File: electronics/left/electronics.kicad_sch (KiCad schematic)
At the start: 85 parts, among them J1 USB_C_Receptacle_USB2.0, J2 Battery Connector, SW1 SW_Reset, U1 Choc v1 Socket, U10 Choc v1 Socket, U11 Choc v1 Socket, U12 Choc v1 Socket, U13 Choc v1 Socket, U14 Choc v1 Socket, U15 Choc v1 Socket, U16 Choc v1 Socket, U17 Choc v1 Socket, U18 Choc v1 Socket, U19 Choc v1 Socket, U2 Choc v1 Socket, U20 Choc v1 Socket, U21 Choc v1 Socket, U22 nRF52840, U23 ESDR0502NMUTAG, U24 BQ24075RGT, U3 Choc v1 Socket, U4 Choc v1 Socket, U5 Choc v1 Socket, U6 Choc v1 Socket, U7 Choc v1 Socket, U8 Choc v1 Socket, U9 Choc v1 Socket, Y1 32.768 kHz, Y2 32MHz

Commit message: Component metadata updates:
* Use official footprints for 0402 caps and resistors.
* Use correct JLC and LCSC part numbers for the choc switches.
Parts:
- C1, C10, C11, C12, C13, C14, C15, C16, C17, C18, C19, C2, C20, C21, C22, C23, C24, C25, C26, C3, C4, C5, C6, C7, C8, C9: footprint lib:C_0402_1005Metric -> Capacitor_SMD:C_0402_1005Metric
- R1, R10, R11, R12, R2, R3, R4, R5, R6, R7, R8, R9: footprint lib:R_0402_1005Metric -> Resistor_SMD:R_0402_1005Metric
- U1, U10, U11, U12, U13, U14, U15, U16, U17, U18, U19, U2, U20, U21, U3, U4, U5, U6, U7, U8, U9: value Choc v1 Socket -> CPG135001S30; JLC Part C2803348 -> C5333465; LCSC Part C2803348 -> C5333465

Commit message: Value update for battery connector and reset switch.
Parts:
- J2: value Battery Connector -> Molex_781710002; symbol Molex_Pico-EZmate_78171-0002_1x02-1MP_P1.20mm_Vertical:Battery Connector -> Molex_Pico-EZmate_78171-0002_1x02-1MP_P1.20mm_Vertical:Molex_781710002
- SW1: value SW_Reset -> EVQPUC02K
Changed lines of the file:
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@@
     )
   )
-  (symbol (lib_id "Molex_Pico-EZmate_78171-0002_1x02-1MP_P1.20mm_Vertical:Battery Connector") (at 249.428 309.88 180) (unit 1)
+  (symbol (lib_id "Molex_Pico-EZmate_78171-0002_1x02-1MP_P1.20mm_Vertical:Molex_781710002") (at 249.428 309.88 180) (unit 1)
     (in_bom yes) (on_board yes) (dnp no)
     (property "Reference" "J2" (at 249.428 299.085 0)
       (effects (font (size 1.27 1.27)))
     )
-    (property "Value" "Battery Connector" (at 249.428 301.625 0)
+    (property "Value" "Molex_781710002" (at 249.555 302.006 0)
       (effects (font (size 1.27 1.27)))
     )
@@
       (effects (font (size 1.27 1.27)) hide)
     )
-    (property "Manufacturer Part" "Molex_Pico-EZmate_78171-0002" (at 249.428 295.91 0)
-      (effects (font (size 1.27 1.27)) hide)
-    )
-    (property "LCSC Part" "C505023" (at 249.428 309.88 0)
-      (effects (font (size 1.27 1.27)) hide)
-    )
-    (property "JLC Part" "C505023" (at 249.428 309.88 0)
+    (property "Manufacturer Part" "Molex_Pico-EZmate_78171-0002" (at 248.793 292.735 0)
+      (effects (font (size 1.27 1.27)) hide)
+    )
+    (property "LCSC Part" "C505023" (at 250.063 295.91 0)
+      (effects (font (size 1.27 1.27)) hide)
+    )
+    (property "JLC Part" "C505023" (at 250.063 295.91 0)
       (effects (font (size 1.27 1.27)) hide)
     )
@@
       (effects (font (size 1.27 1.27)) (justify right))
     )
-    (property "Value" "SW_Reset" (at 60.96 254 0)
+    (property "Value" "EVQPUC02K" (at 60.96 254 0)
       (effects (font (size 1.27 1.27)) (justify right))
     )
@@
       (effects (font (size 1.27 1.27)) hide)
     )
-    (property "Datasheet" "~" (at 57.15 257.81 0)
-      (effects (font (size 1.27 1.27)) hide)
-    )
+    (property "Datasheet" "" (at 57.15 257.81 0)
+      (effects (font (size 1.27 1.27)) hide)
+    )

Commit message: BOM value updates:
USB C Receptable
Molex connector.
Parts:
- J1: LCSC Part (none) -> C2988367; Manufacturer Part (none) -> GT-USB-9014C
- J2: Manufacturer Part Molex_Pico-EZmate_78171-0002 -> 781710002
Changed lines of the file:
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@@
       (effects (font (size 1.27 1.27)) hide)
     )
-    (property "Manufacturer Part" "Molex_Pico-EZmate_78171-0002" (at 248.793 292.735 0)
+    (property "Manufacturer Part" "781710002" (at 248.793 292.735 0)
       (effects (font (size 1.27 1.27)) hide)
     )
@@
       (effects (font (size 1.27 1.27)) hide)
     )
+    (property "LCSC Part" "C2988367" (at 192.405 253.746 90)
+      (effects (font (size 1.27 1.27)) hide)
+    )
+    (property "Manufacturer Part" "GT-USB-9014C" (at 192.405 253.746 90)
+      (effects (font (size 1.27 1.27)) hide)
+    )

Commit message: Add JLC Part number to LEDs
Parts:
- D1: JLC Part (none) -> C605447
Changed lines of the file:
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@@
+      (effects (font (size 1.27 1.27)) hide)
+    )
+    (property "JLC Part" "C605447" (at 189.23 189.23 0)
       (effects (font (size 1.27 1.27)) hide)
     )

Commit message: Use official symbol for charging IC.
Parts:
- U24: footprint lib:VQFN-16-1EP_3x3mm_P0.5mm_EP1.6x1.6mm -> Package_DFN_QFN:VQFN-16-1EP_3x3mm_P0.5mm_EP1.6x1.6mm; symbol BQ24075RGT:BQ24075RGT -> Battery_Management:BQ24075RGT
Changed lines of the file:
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@@
     )
   )
-  (symbol (lib_id "BQ24075RGT:BQ24075RGT") (at 204.343 327.66 0) (unit 1)
+  (symbol (lib_id "Battery_Management:BQ24075RGT") (at 204.343 327.66 0) (unit 1)
     (in_bom yes) (on_board yes) (dnp no)
     (property "Reference" "U24" (at 202.438 347.345 0)
@@
       (effects (font (size 1.27 1.27)) (justify left))
     )
-    (property "Footprint" "lib:VQFN-16-1EP_3x3mm_P0.5mm_EP1.6x1.6mm" (at 211.963 341.63 0)
+    (property "Footprint" "Package_DFN_QFN:VQFN-16-1EP_3x3mm_P0.5mm_EP1.6x1.6mm" (at 211.963 341.63 0)
       (effects (font (size 1.27 1.27)) (justify left) hide)
     )

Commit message: electronics/right: Fix schema and PCB references parity.
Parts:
- renumbered U1 to SW1, U10 to SW10, U11 to SW11, U12 to SW12, U13 to SW13, U14 to SW14, U15 to SW15, U16 to SW16, U17 to SW17, U18 to SW18, U19 to SW19, U2 to SW2, U20 to SW20, U21 to SW21, U3 to SW3, U4 to SW4, U5 to SW5, U6 to SW6, U7 to SW7, U8 to SW8, U9 to SW9
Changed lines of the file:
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@@
   (symbol (lib_id "Kailh_socket_PG1350:Choc v1 Socket") (at 262.89 30.48 0) (unit 1)
     (in_bom yes) (on_board yes) (dnp no) (fields_autoplaced)
-    (property "Reference" "U6" (at 263.525 21.751 0)
+    (property "Reference" "SW6" (at 263.525 21.751 0)
       (effects (font (size 1.27 1.27)))
     )
@@
   (symbol (lib_id "Kailh_socket_PG1350:Choc v1 Socket") (at 179.07 60.96 0) (unit 1)
     (in_bom yes) (on_board yes) (dnp no) (fields_autoplaced)
-    (property "Reference" "U15" (at 179.705 52.231 0)
+    (property "Reference" "SW15" (at 179.705 52.231 0)
       (effects (font (size 1.27 1.27)))
     )
@@
   (symbol (lib_id "Kailh_socket_PG1350:Choc v1 Socket") (at 120.65 60.96 0) (unit 1)
     (in_bom yes) (on_board yes) (dnp no) (fields_autoplaced)
-    (property "Reference" "U13" (at 121.285 51.435 0)
+    (property "Reference" "SW13" (at 121.285 51.435 0)
       (effects (font (size 1.27 1.27)))
     )
@@
   (symbol (lib_id "Kailh_socket_PG1350:Choc v1 Socket") (at 262.89 60.96 0) (unit 1)
     (in_bom yes) (on_board yes) (dnp no) (fields_autoplaced)
-    (property "Reference" "U18" (at 263.525 52.231 0)
+    (property "Reference" "SW18" (at 263.525 52.231 0)
       (effects (font (size 1.27 1.27)))
     )
@@
   (symbol (lib_id "Kailh_socket_PG1350:Choc v1 Socket") (at 236.22 76.2 0) (unit 1)
     (in_bom yes) (on_board yes) (dnp no) (fields_autoplaced)
-    (property "Reference" "U20" (at 236.855 67.471 0)
+    (property "Reference" "SW20" (at 236.855 67.471 0)
       (effects (font (size 1.27 1.27)))
     )
@@
   (symbol (lib_id "Kailh_socket_PG1350:Choc v1 Socket") (at 149.86 60.96 0) (unit 1)
     (in_bom yes) (on_board yes) (dnp no) (fields_autoplaced)
-    (property "Reference" "U14" (at 150.495 52.231 0)
+    (property "Reference" "SW14" (at 150.495 52.231 0)
       (effects (font (size 1.27 1.27)))
     )
@@
   (symbol (lib_id "Kailh_socket_PG1350:Choc v1 Socket") (at 149.86 45.72 0) (unit 1)
     (in_bom yes) (on_board yes) (dnp no) (fields_autoplaced)
-    (property "Reference" "U8" (at 150.495 36.991 0)
+    (property "Reference" "SW8" (at 150.495 36.991 0)
       (effects (font (size 1.27 1.27)))
     )
@@
   (symbol (lib_id "Kailh_socket_PG1350:Choc v1 Socket") (at 234.95 45.72 0) (unit 1)
     (in_bom yes) (on_board yes) (dnp no) (fields_autoplaced)
-    (property "Reference" "U11" (at 235.585 36.991 0)
+    (property "Reference" "SW11" (at 235.585 36.991 0)
       (effects (font (size 1.27 1.27)))
     )
@@
   (symbol (lib_id "Kailh_socket_PG1350:Choc v1 Socket") (at 234.95 30.48 0) (unit 1)
     (in_bom yes) (on_board yes) (dnp no) (fields_autoplaced)
-    (property "Reference" "U5" (at 235.585 20.955 0)
+    (property "Reference" "SW5" (at 235.585 20.955 0)
       (effects (font (size 1.27 1.27)))
     )
@@
   (symbol (lib_id "Kailh_socket_PG1350:Choc v1 Socket") (at 208.28 60.96 0) (unit 1)
     (in_bom yes) (on_board yes) (dnp no) (fields_autoplaced)
-    (property "Reference" "U16" (at 208.915 52.231 0)
+    (property "Reference" "SW16" (at 208.915 52.231 0)
       (effects (font (size 1.27 1.27)))
     )
@@
   (symbol (lib_id "Kailh_socket_PG1350:Choc v1 Socket") (at 236.22 60.96 0) (unit 1)
     (in_bom yes) (on_board yes) (dnp no) (fields_autoplaced)
-    (property "Reference" "U17" (at 236.855 52.231 0)
+    (property "Reference" "SW17" (at 236.855 52.231 0)
       (effects (font (size 1.27 1.27)))
     )
@@
   (symbol (lib_id "Kailh_socket_PG1350:Choc v1 Socket") (at 208.28 45.72 0) (unit 1)
     (in_bom yes) (on_board yes) (dnp no) (fields_autoplaced)
-    (property "Reference" "U10" (at 208.915 36.991 0)
+    (property "Reference" "SW10" (at 208.915 36.991 0)
       (effects (font (size 1.27 1.27)))
     )
@@
   (symbol (lib_id "Kailh_socket_PG1350:Choc v1 Socket") (at 179.07 30.48 0) (unit 1)
     (in_bom yes) (on_board yes) (dnp no) (fields_autoplaced)
-    (property "Reference" "U3" (at 179.705 21.751 0)
+    (property "Reference" "SW3" (at 179.705 21.751 0)
       (effects (font (size 1.27 1.27)))
     )
@@
   (symbol (lib_id "Kailh_socket_PG1350:Choc v1 Socket") (at 207.01 30.48 0) (unit 1)
     (in_bom yes) (on_board yes) (dnp no) (fields_autoplaced)
-    (property "Reference" "U4" (at 207.645 21.751 0)
+    (property "Reference" "SW4" (at 207.645 21.751 0)
       (effects (font (size 1.27 1.27)))
     )
@@
   (symbol (lib_id "Kailh_socket_PG1350:Choc v1 Socket") (at 208.28 76.2 0) (unit 1)
     (in_bom yes) (on_board yes) (dnp no) (fields_autoplaced)
-    (property "Reference" "U19" (at 208.915 67.471 0)
+    (property "Reference" "SW19" (at 208.915 67.471 0)
       (effects (font (size 1.27 1.27)))
     )
@@
   (symbol (lib_id "Kailh_socket_PG1350:Choc v1 Socket") (at 149.86 30.48 0) (unit 1)
     (in_bom yes) (on_board yes) (dnp no) (fields_autoplaced)
-    (property "Reference" "U2" (at 150.495 21.751 0)
+    (property "Reference" "SW2" (at 150.495 21.751 0)
       (effects (font (size 1.27 1.27)))
     )
@@
   (symbol (lib_id "Kailh_socket_PG1350:Choc v1 Socket") (at 264.16 76.2 0) (unit 1)
     (in_bom yes) (on_board yes) (dnp no) (fields_autoplaced)
-    (property "Reference" "U21" (at 264.795 67.471 0)
+    (property "Reference" "SW21" (at 264.795 67.471 0)
       (effects (font (size 1.27 1.27)))
     )
@@
   (symbol (lib_id "Kailh_socket_PG1350:Choc v1 Socket") (at 262.89 45.72 0) (unit 1)
     (in_bom yes) (on_board yes) (dnp no) (fields_autoplaced)
-    (property "Reference" "U12" (at 263.525 36.195 0)
+    (property "Reference" "SW12" (at 263.525 36.195 0)
       (effects (font (size 1.27 1.27)))
     )
@@
   (symbol (lib_id "Kailh_socket_PG1350:Choc v1 Socket") (at 120.65 30.48 0) (unit 1)
     (in_bom yes) (on_board yes) (dnp no) (fields_autoplaced)
-    (property "Reference" "U1" (at 121.285 20.955 0)
+    (property "Reference" "SW1" (at 121.285 20.955 0)
       (effects (font (size 1.27 1.27)))
     )
@@
   (symbol (lib_id "Kailh_socket_PG1350:Choc v1 Socket") (at 179.07 45.72 0) (unit 1)
     (in_bom yes) (on_board yes) (dnp no) (fields_autoplaced)
-    (property "Reference" "U9" (at 179.705 36.991 0)
+    (property "Reference" "SW9" (at 179.705 36.991 0)
       (effects (font (size 1.27 1.27)))
     )
@@
   (symbol (lib_id "Kailh_socket_PG1350:Choc v1 Socket") (at 120.65 45.72 0) (unit 1)
     (in_bom yes) (on_board yes) (dnp no) (fields_autoplaced)
-    (property "Reference" "U7" (at 121.285 36.195 0)
+    (property "Reference" "SW7" (at 121.285 36.195 0)
       (effects (font (size 1.27 1.27)))
     )

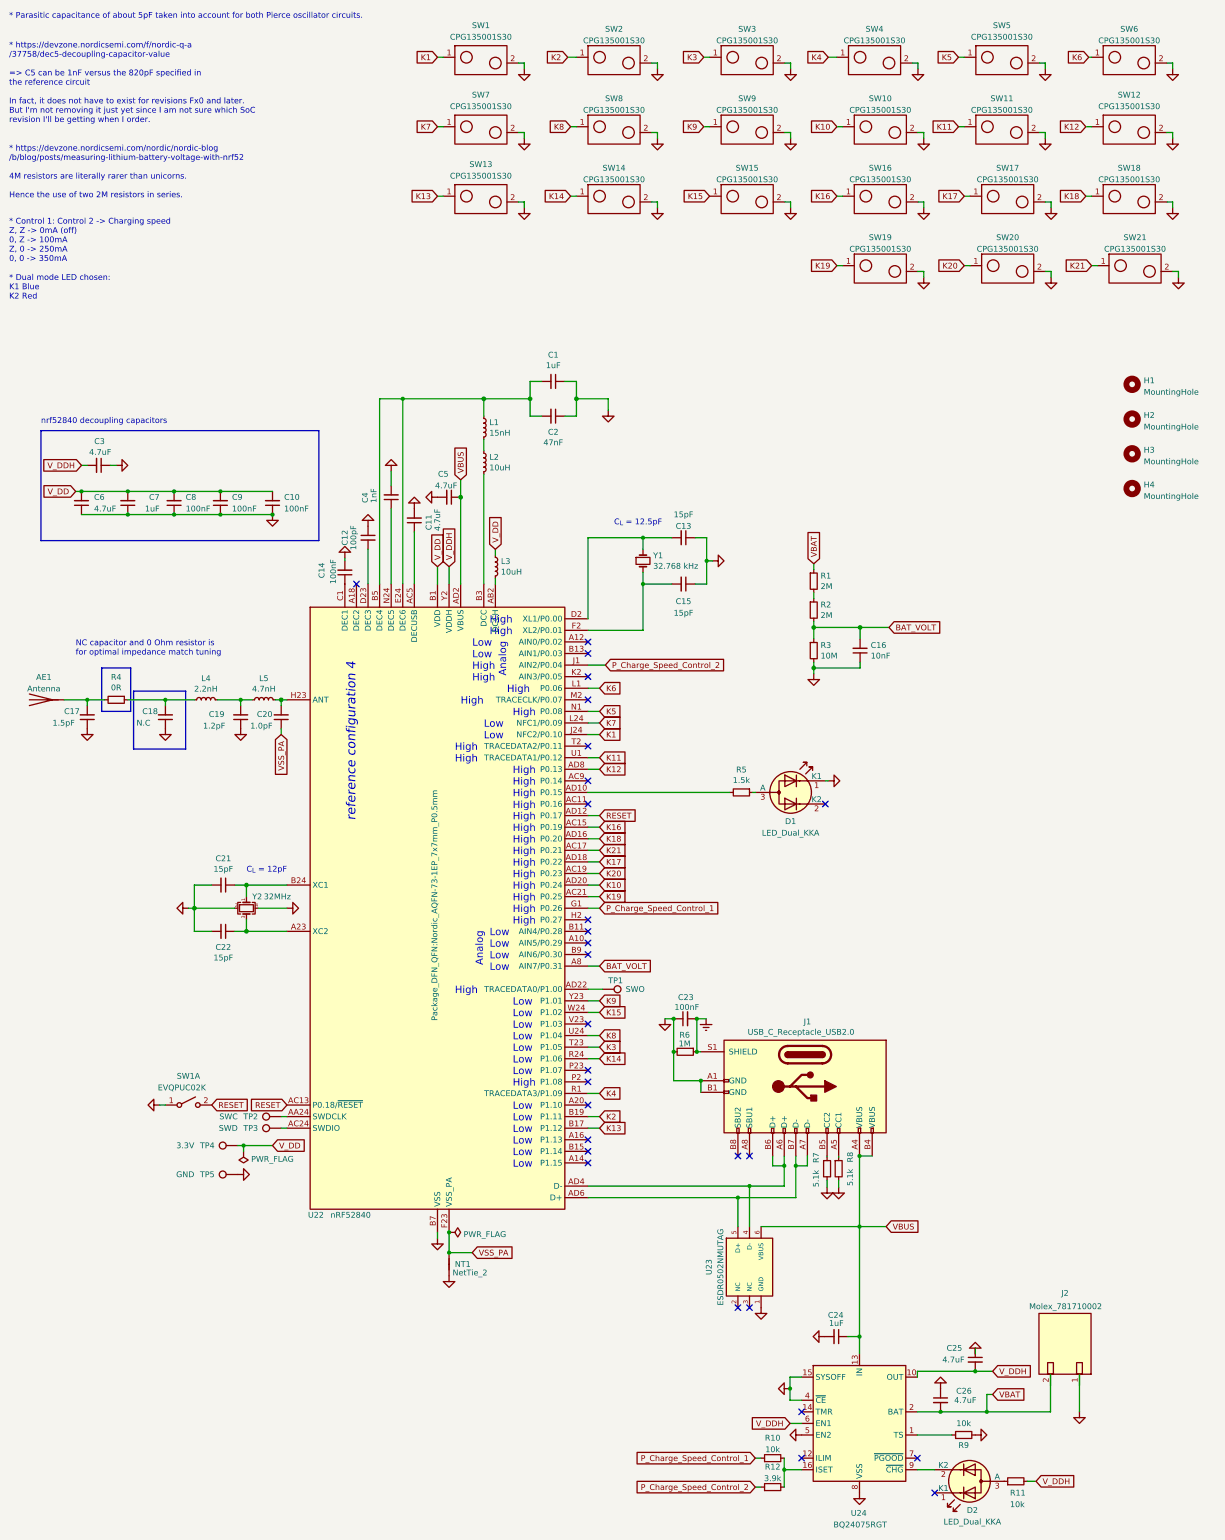
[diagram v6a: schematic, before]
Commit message: electronics/left: Fix schema and PCB references parity.
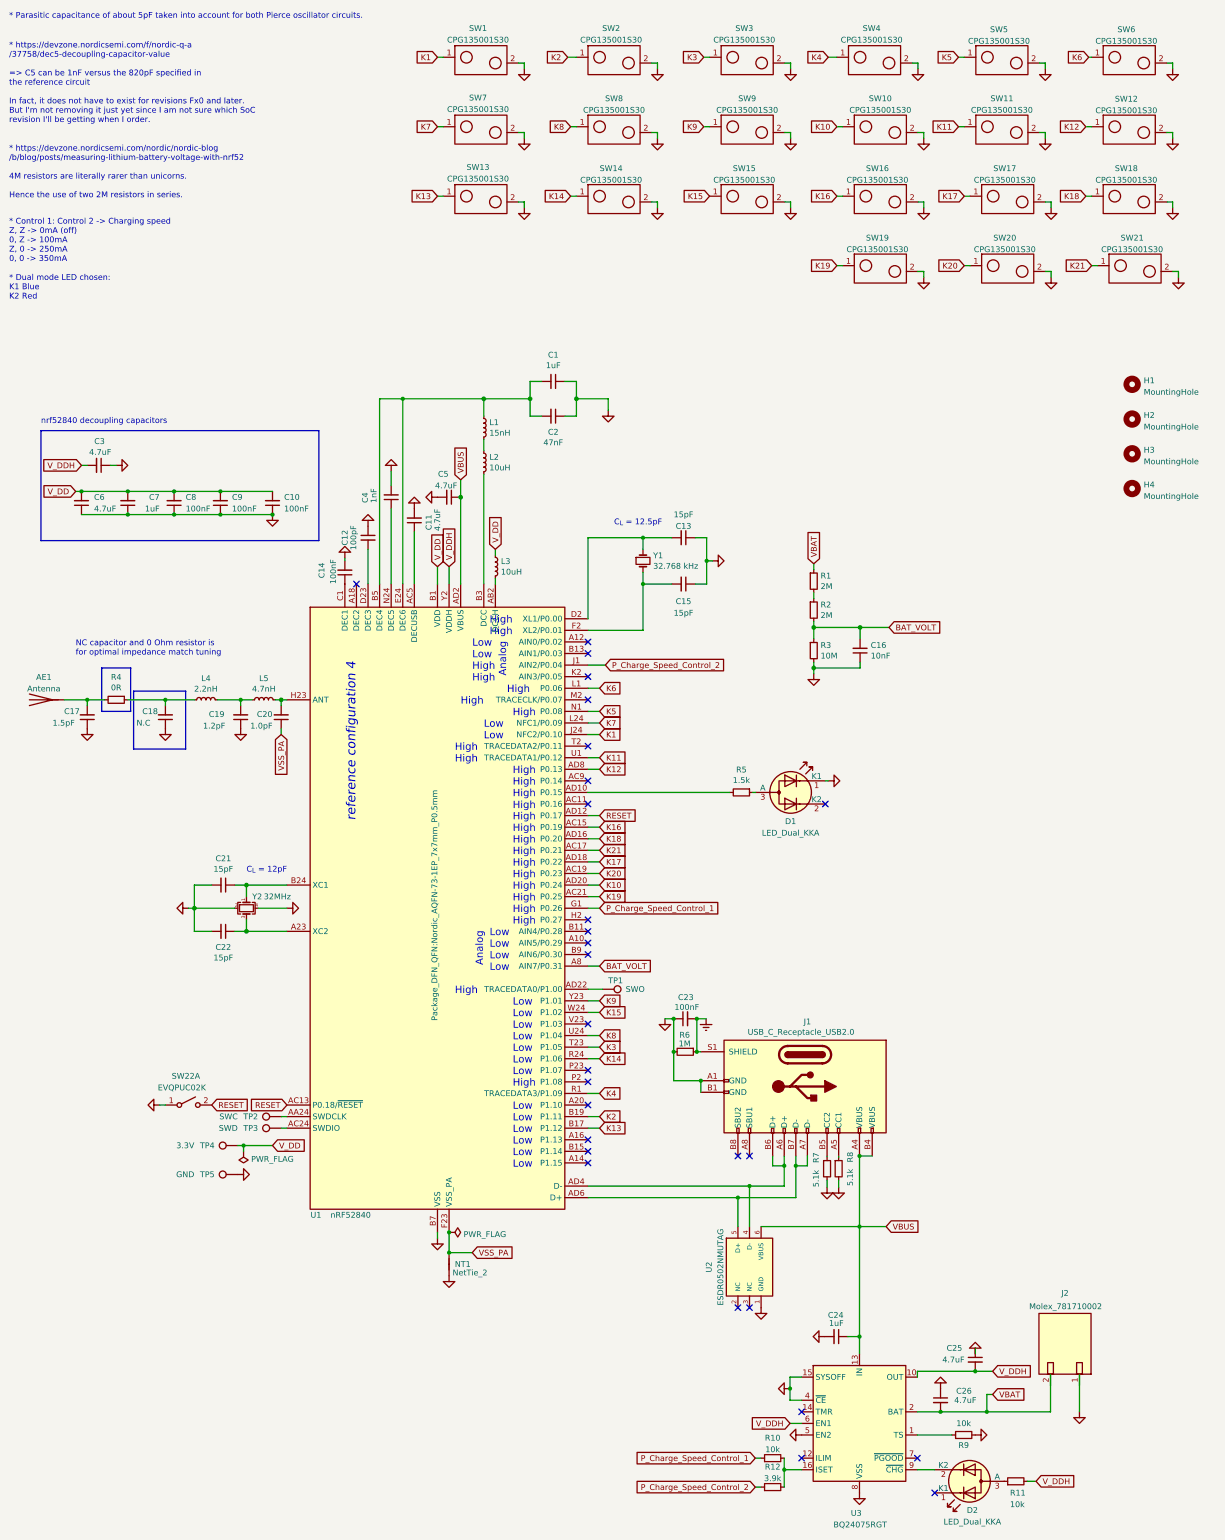
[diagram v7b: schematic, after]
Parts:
- renumbered SW1 to SW22, U22 to U1, U23 to U2, U24 to U3
